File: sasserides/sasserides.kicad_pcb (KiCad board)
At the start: 2 copper layers, 170 x 80 mm, 133 parts, among them J1 Conn_02x16_Odd_Even, Q1 2N7002, U1 CDCV304PW

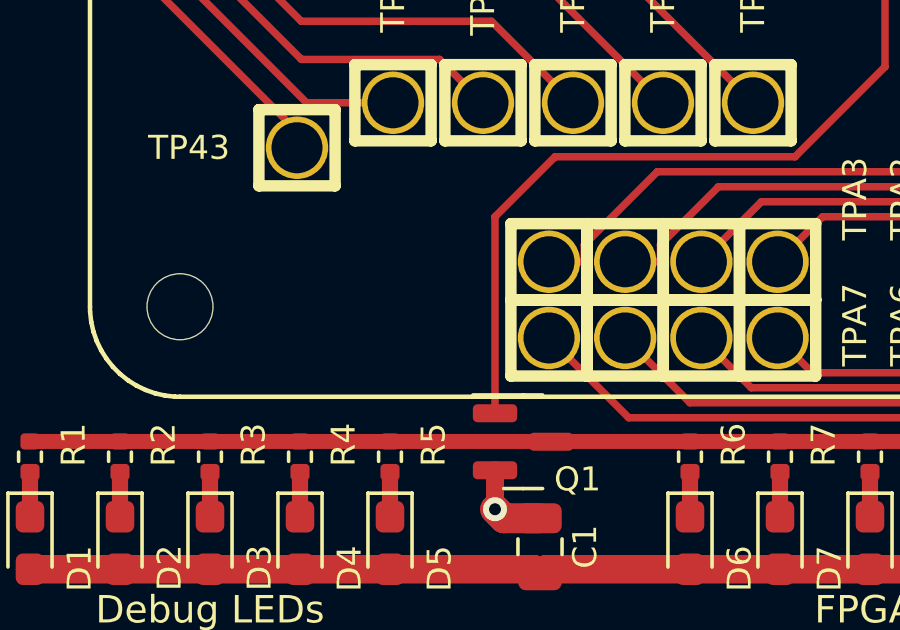
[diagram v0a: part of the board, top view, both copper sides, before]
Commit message: Add 10k pulldown to Q1 gate.
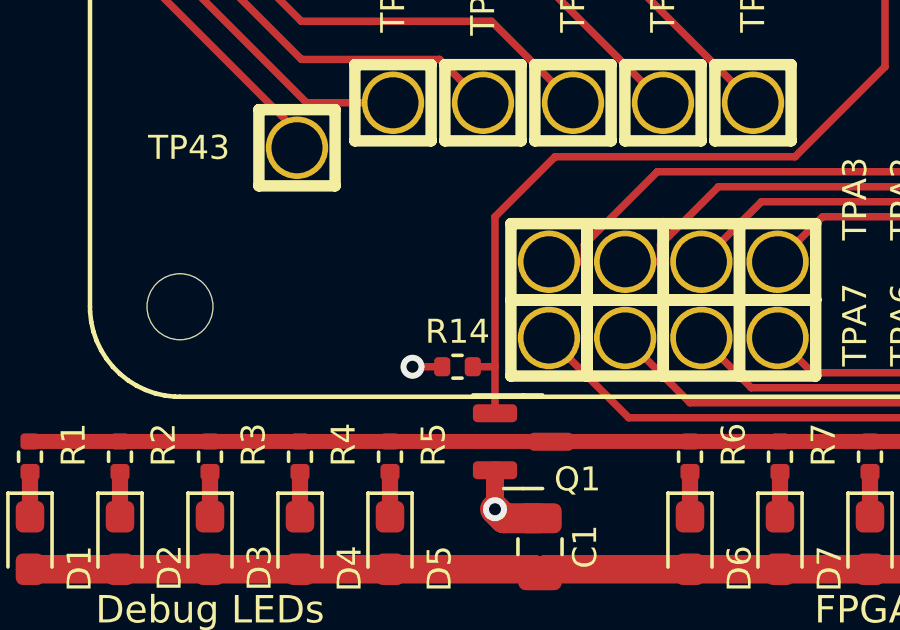
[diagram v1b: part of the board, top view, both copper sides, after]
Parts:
- added R14: 10k, Resistor_SMD:R_0402_1005Metric, F.Cu at (84.2, 131.0)
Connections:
- net REF_LED_EN renamed /REF_LED_EN
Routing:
- net GND: track 8.41 -> 9.39 mm, vias 3 -> 4
- net /REF_LED_EN: track 97.9 -> 98.6 mm
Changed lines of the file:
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@@
   (net 31 "/+5V")
   (net 32 "/D11 Vf")
-  (net 33 "REF_LED_EN")
+  (net 33 "/REF_LED_EN")
   (net 34 "GND")
   (net 35 "Net-(Q1-D)")
@@
       (net 90 "/CLK_BUF") (pinfunction "Pin_31") (pintype "passive"))
     (pad "32" thru_hole oval (at 1.265 17.775 90) (size 1.7 1.7) (drill 1) (layers "*.Cu" "*.Mask")
-      (net 33 "REF_LED_EN") (pinfunction "Pin_32") (pintype "passive"))
+      (net 33 "/REF_LED_EN") (pinfunction "Pin_32") (pintype "passive"))
     (pad "33" thru_hole oval (at -1.275 20.315 90) (size 1.7 1.7) (drill 1) (layers "*.Cu" "*.Mask")
       (net 2 "VCC") (pinfunction "Pin_33") (pintype "passive"))
@@
       (stroke (width 0.1) (type solid)) (layer "F.Fab"))
     (pad "1" smd roundrect (at -0.9375 -0.95) (size 1.475 0.6) (layers "F.Cu" "F.Paste" "F.Mask") (roundrect_rratio 0.25)
-      (net 33 "REF_LED_EN") (pinfunction "G") (pintype "input"))
+      (net 33 "/REF_LED_EN") (pinfunction "G") (pintype "input"))
     (pad "2" smd roundrect (at -0.9375 0.95) (size 1.475 0.6) (layers "F.Cu" "F.Paste" "F.Mask") (roundrect_rratio 0.25)
       (net 34 "GND") (pinfunction "S") (pintype "passive"))
@@
     (pad "" np_thru_hole circle (at 0 0) (size 2.2 2.2) (drill 2.2) (layers "*.Cu" "*.Mask"))
   )
+  (footprint "Resistor_SMD:R_0402_1005Metric" (layer "F.Cu")
+    (at 84.25 131)
+    (descr "Resistor SMD 0402 (1005 Metric), square (rectangular) end terminal, IPC_7351 nominal, (Body size source: IPC-SM-782 page 72, https://www.pcb-3d.com/wordpress/wp-content/uploads/ipc-sm-782a_amendment_1_and_2.pdf), generated with kicad-footprint-generator")
+    (tags "resistor")
+    (property "Description" "RES 10K OHM 5% 1/16W 0402")
+    (property "Manufacturer" "Yageo")
+    (property "Part Number" "RC0402JR-0710KL")
+    (property "Sheetfile" "sasserides.kicad_sch")
+    (property "Sheetname" "")
+    (property "Substitution" "any equivalent")
+    (property "ki_description" "Resistor")
+    (property "ki_keywords" "R res resistor")
+    (attr smd)
+    (fp_text reference "R14" (at 0 -1.17) (layer "F.SilkS")
+        (effects (font (size 0.8 0.8) (thickness 0.15)))
+    )
+    (fp_text value "10k" (at 0 -1.25) (layer "F.Fab")
+        (effects (font (size 1 1) (thickness 0.15)))
+    )
+    (fp_text user "${REFERENCE}" (at 0 0) (layer "F.Fab")
+        (effects (font (size 0.26 0.26) (thickness 0.04)))
+    )
+    (fp_line (start -0.153641 -0.38) (end 0.153641 -0.38)
+      (stroke (width 0.12) (type solid)) (layer "F.SilkS"))
+    (fp_line (start -0.153641 0.38) (end 0.153641 0.38)
+      (stroke (width 0.12) (type solid)) (layer "F.SilkS"))
+    (fp_line (start -0.93 -0.47) (end 0.93 -0.47)
+      (stroke (width 0.05) (type solid)) (layer "F.CrtYd"))
+    (fp_line (start -0.93 0.47) (end -0.93 -0.47)
+      (stroke (width 0.05) (type solid)) (layer "F.CrtYd"))
+    (fp_line (start 0.93 -0.47) (end 0.93 0.47)
+      (stroke (width 0.05) (type solid)) (layer "F.CrtYd"))
+    (fp_line (start 0.93 0.47) (end -0.93 0.47)
+      (stroke (width 0.05) (type solid)) (layer "F.CrtYd"))
+    (fp_line (start -0.525 -0.27) (end 0.525 -0.27)
+      (stroke (width 0.1) (type solid)) (layer "F.Fab"))
+    (fp_line (start -0.525 0.27) (end -0.525 -0.27)
+      (stroke (width 0.1) (type solid)) (layer "F.Fab"))
+    (fp_line (start 0.525 -0.27) (end 0.525 0.27)
+      (stroke (width 0.1) (type solid)) (layer "F.Fab"))
+    (fp_line (start 0.525 0.27) (end -0.525 0.27)
+      (stroke (width 0.1) (type solid)) (layer "F.Fab"))
+    (pad "1" smd roundrect (at -0.51 0) (size 0.54 0.64) (layers "F.Cu" "F.Paste" "F.Mask") (roundrect_rratio 0.25)
+      (net 34 "GND") (pintype "passive"))
+    (pad "2" smd roundrect (at 0.51 0) (size 0.54 0.64) (layers "F.Cu" "F.Paste" "F.Mask") (roundrect_rratio 0.25)
+      (net 33 "/REF_LED_EN") (pintype "passive"))
+    (model "${KICAD6_3DMODEL_DIR}/Resistor_SMD.3dshapes/R_0402_1005Metric.wrl"
+      (offset (xyz 0 0 0))
+      (scale (xyz 1 1 1))
+      (rotate (xyz 0 0 0))
+    )
+  )
   (footprint "tycho:HEADER-1x1-TESTPROBE" (layer "F.Cu")
     (at 178.6 102)
@@
   (segment (start 116.515 68.68) (end 116.515 70.75) (width 0.25) (layer "F.Cu") (net 33))
   (segment (start 95.5 124) (end 87.5 124) (width 0.25) (layer "F.Cu") (net 33))
-  (segment (start 85.5 126) (end 85.5 132.55) (width 0.25) (layer "F.Cu") (net 33))
   (segment (start 108.875 113) (end 108.125 112.25) (width 0.25) (layer "F.Cu") (net 33))
   (segment (start 114.75 86.5) (end 123.75 95.5) (width 0.25) (layer "F.Cu") (net 33))
@@
   (segment (start 98.5 115.25) (end 98.5 121) (width 0.25) (layer "F.Cu") (net 33))
   (segment (start 123.75 101.25) (end 112 113) (width 0.25) (layer "F.Cu") (net 33))
+  (segment (start 85.5 126) (end 85.5 131) (width 0.25) (layer "F.Cu") (net 33))
   (segment (start 98.5 121) (end 95.5 124) (width 0.25) (layer "F.Cu") (net 33))
+  (segment (start 85.5 131) (end 85.5 132.55) (width 0.25) (layer "F.Cu") (net 33))
   (segment (start 117.78 67.415) (end 116.515 68.68) (width 0.25) (layer "F.Cu") (net 33))
+  (segment (start 84.75 131) (end 85.5 131) (width 0.25) (layer "F.Cu") (net 33))
   (segment (start 108.125 112.25) (end 101.5 112.25) (width 0.25) (layer "F.Cu") (net 33))
   (segment (start 101.5 112.25) (end 98.5 115.25) (width 0.25) (layer "F.Cu") (net 33))
@@
   (segment (start 108.225 117.725) (end 107.1375 117.725) (width 0.4) (layer "F.Cu") (net 34))
   (segment (start 87 136.05) (end 85.8 136.05) (width 1) (layer "F.Cu") (net 34))
+  (segment (start 83.73 131) (end 82.75 131) (width 0.25) (layer "F.Cu") (net 34))
   (segment (start 109.05 118.55) (end 108.225 117.725) (width 0.4) (layer "F.Cu") (net 34))
   (segment (start 109.05 119.75) (end 107.8 119.75) (width 0.95) (layer "F.Cu") (net 34))
   (segment (start 85.8 136.05) (end 85.5 135.75) (width 1) (layer "F.Cu") (net 34))
   (segment (start 105.6 114.78) (end 105.6 114) (width 0.25) (layer "F.Cu") (net 34))
+  (via (at 82.75 131) (size 0.8) (drill 0.4) (layers "F.Cu" "B.Cu") (net 34))
   (via (at 107.8 119.75) (size 0.8) (drill 0.4) (layers "F.Cu" "B.Cu") (net 34))
   (via (at 105.6 114) (size 0.8) (drill 0.4) (layers "F.Cu" "B.Cu") (net 34))

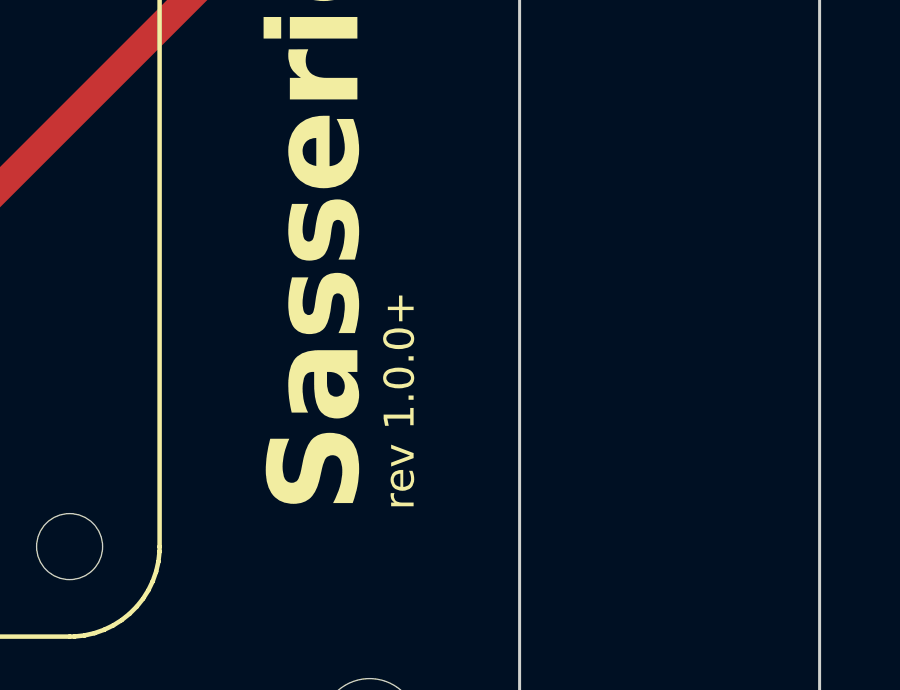
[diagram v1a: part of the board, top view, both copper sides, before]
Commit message: Update DATE and add date to Sasserides-A silkscreen.
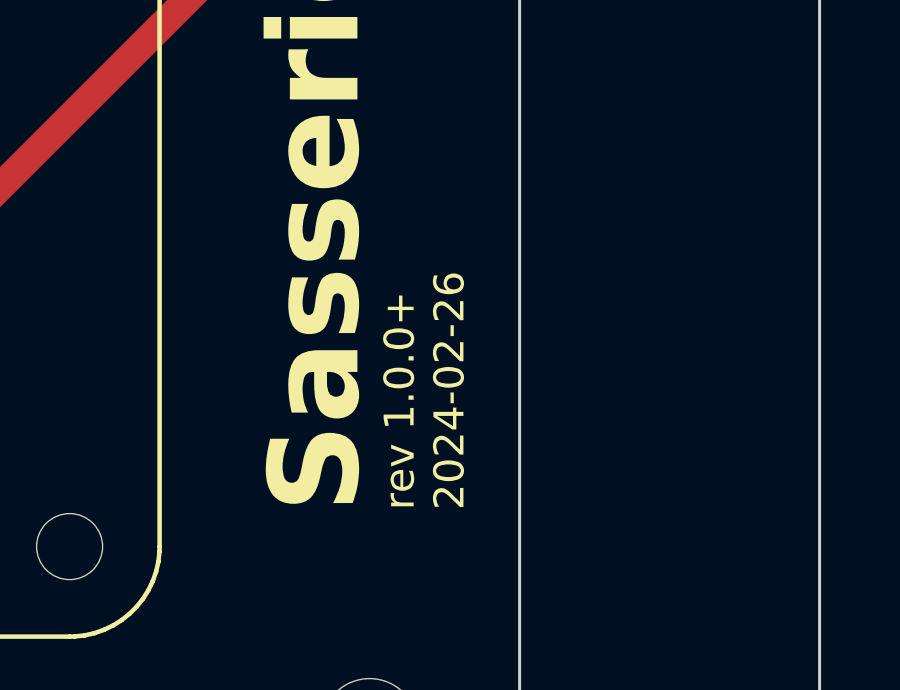
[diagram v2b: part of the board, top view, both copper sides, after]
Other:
- board text added: "2024-02-26"
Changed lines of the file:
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@@
     )
   )
-  (property "DATE" "2023-05-25")
+  (property "DATE" "2024-02-26")
   (property "VERSION" "r1.0.0+")
   (net 0 "")
@@
     (effects (font (size 0.9144 0.9238) (thickness 0.15)))
   )
+  (gr_text "2024-02-26" (at 138.25 127.78 90) (layer "F.SilkS")
+    (effects (font (size 1 1) (thickness 0.15)) (justify left bottom))
+  )
   (gr_text "Debug LEDs" (at 76 139.1) (layer "F.SilkS")

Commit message: Update Sasserides PCB
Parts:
- C1, C2: footprint Capacitor_SMD:C_0805_2012Metric -> Capacitor_SMD:C_0603_1608Metric_Pad1.08x0.95mm_HandSolder

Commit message: Update date
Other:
- board text added: "2024-03-04"
- board text removed: "2024-02-26"
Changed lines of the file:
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@@
     (effects (font (size 0.9144 0.9238) (thickness 0.15)))
   )
-  (gr_text "2024-02-26" (at 138.25 127.78 90) (layer "F.SilkS")
+  (gr_text "2024-03-04" (at 138.25 127.78 90) (layer "F.SilkS")
     (effects (font (size 1 1) (thickness 0.15)) (justify left bottom))
   )

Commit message: Bump Sasserides schematic/Sasserides-A to r1.0.1; Update date
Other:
- board text added: "2024-03-07"
- board text added: "rev 1.0.1"
- board text removed: "2024-03-04"
- board text removed: "rev 1.0.0+"
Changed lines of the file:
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@@
     )
   )
-  (property "DATE" "2024-02-26")
-  (property "VERSION" "r1.0.0+")
+  (property "DATE" "2024-03-07")
+  (property "VERSION" "r1.0.1")
   (net 0 "")
   (net 1 "Net-(D1-K)")
@@
   (gr_rect (start 60 60) (end 140 140)
     (stroke (width 0.1) (type default)) (fill none) (layer "Edge.Cuts"))
-  (gr_text "rev 1.0.0+" (at 136.59 127.78 90) (layer "F.SilkS")
+  (gr_text "rev 1.0.1" (at 136.59 127.78 90) (layer "F.SilkS")
     (effects (font (size 1 1) (thickness 0.15)) (justify left bottom))
   )
@@
     (effects (font (size 0.9144 0.9238) (thickness 0.15)))
   )
-  (gr_text "2024-03-04" (at 138.25 127.78 90) (layer "F.SilkS")
+  (gr_text "2024-03-07" (at 138.25 127.78 90) (layer "F.SilkS")
     (effects (font (size 1 1) (thickness 0.15)) (justify left bottom))
   )
